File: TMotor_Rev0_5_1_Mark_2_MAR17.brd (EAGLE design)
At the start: 88.9 x 79.4 mm, 64 parts, among them U10 DEV-16771, U3 INA125U, U4 INA125U, U5 SN65HVD230MDREP

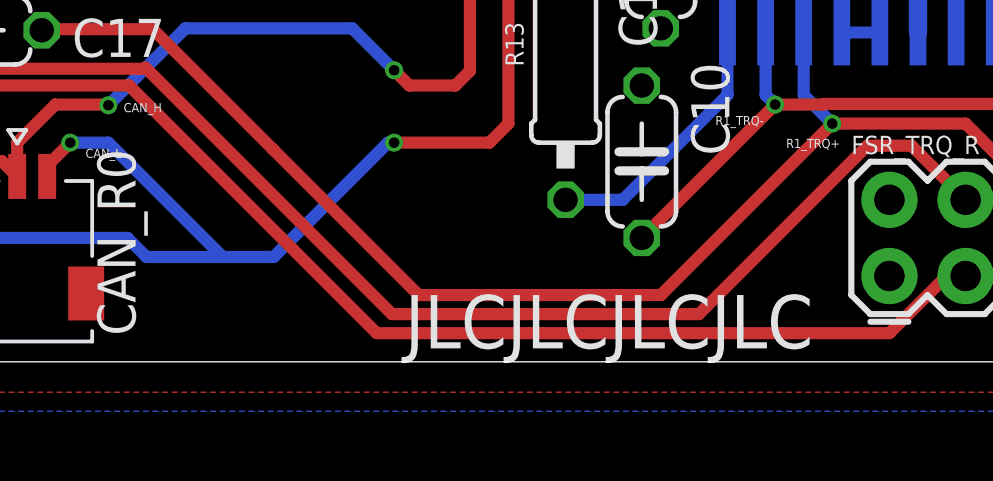
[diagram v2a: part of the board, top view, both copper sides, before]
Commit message: Replaced the CAN transceiver
Replaced SN65HVD230MDREP with SN65HVD230DR
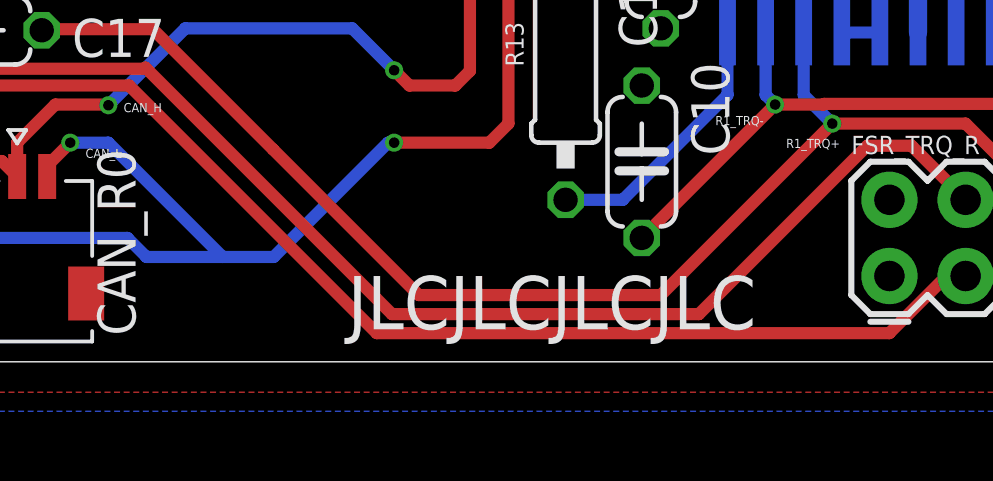
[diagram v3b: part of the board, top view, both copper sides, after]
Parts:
- U5: value SN65HVD230MDREP -> SN65HVD230DR; device SnapEDA-Library:SOIC127P599X175-8N -> SN65HVD230DR:SOIC127P599X175-8N
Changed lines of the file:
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@@
 <vertex x="13.97" y="19.05"/>
 </polygon>
-<text x="24.13" y="6.985" size="1.778" layer="121" rot="R180">JLCJLCJLCJLC</text>
+<text x="22.225" y="7.62" size="1.778" layer="121" rot="R180">JLCJLCJLCJLC</text>
 <polygon width="0" layer="121">
 <vertex x="-0.635" y="60.325"/>
@@
 <attribute name="VENDOR" value="Texas Instruments" x="11.1125" y="1.27" size="1.778" layer="28" rot="MR90" display="off"/>
 </element>
-<element name="U5" library="SnapEDA-Library" package="SOIC127P599X175-8N" value="SN65HVD230MDREP" x="1.5875" y="56.1975" smashed="yes" rot="MR180">
+<element name="U5" library="SN65HVD230DR" package="SOIC127P599X175-8N" value="SN65HVD230DR" x="1.5875" y="56.1975" smashed="yes" rot="MR180">
+<attribute name="AVAILABILITY" value="In Stock" x="1.5875" y="56.1975" size="1.778" layer="28" rot="MR180" display="off"/>
+<attribute name="DESCRIPTION" value=" 3.3 V CAN Transceiver with Standby Mode " x="1.5875" y="56.1975" size="1.778" layer="28" rot="MR180" display="off"/>
+<attribute name="MF" value="Texas Instruments" x="1.5875" y="56.1975" size="1.778" layer="28" rot="MR180" display="off"/>
+<attribute name="MP" value="SN65HVD230DR" x="1.5875" y="56.1975" size="1.778" layer="28" rot="MR180" display="off"/>
+<attribute name="PACKAGE" value="SOIC-8 Texas Instruments" x="1.5875" y="56.1975" size="1.778" layer="28" rot="MR180" display="off"/>
+<attribute name="PRICE" value="None" x="1.5875" y="56.1975" size="1.778" layer="28" rot="MR180" display="off"/>
+<attribute name="PURCHASE-URL" value="https://pricing.snapeda.com/search/part/SN65HVD230DR/?ref=eda" x="1.5875" y="56.1975" size="1.778" layer="28" rot="MR180" display="off"/>
 <attribute name="VALUE" x="6.3055" y="46.9225" size="1.27" layer="28" rot="MR90" align="top-left"/>
 </element>
